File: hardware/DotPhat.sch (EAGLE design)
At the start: 46 parts, among them CN1 1X4-BIG, IC1 CAT24M010TS, J2 RASPBERRYPI-40-PIN-GPIO_PTH, J3 USB-MICROB, U1 ATMEGA328P-MU-QFN32, U2 TMP102, U3 ATSHA204-TSU, U4 W25Q32FV, X2 MC-RTC-RV-4162-C7-I2C, X3 S4B-ZR

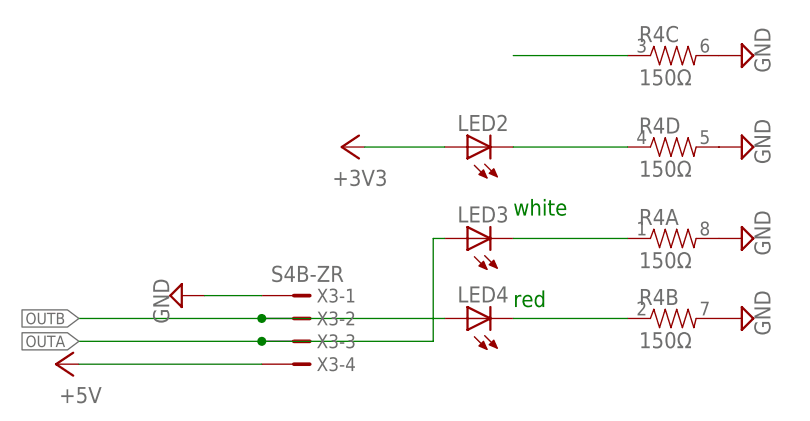
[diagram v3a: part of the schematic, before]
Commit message: Add jumper for power led
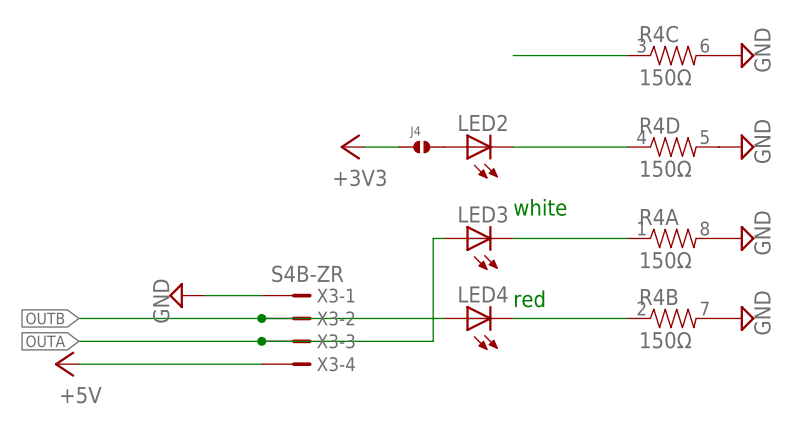
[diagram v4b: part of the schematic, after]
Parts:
- added J4: (no value), solderjumper:SOLDERJUMPER.2.MED
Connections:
- new net N$12: J4.2, LED2.A
- net +3V3: now also J4.1; no longer LED2.A
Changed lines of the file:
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@@
 <setting verticaltext="up"/>
 </settings>
-<grid distance="0.1" unitdist="inch" unit="inch" style="lines" multiple="1" display="no" altdistance="0.01" altunitdist="inch" altunit="inch"/>
+<grid distance="0.05" unitdist="inch" unit="inch" style="lines" multiple="1" display="no" altdistance="0.01" altunitdist="inch" altunit="inch"/>
 <layers>
 <layer number="1" name="Top" color="4" fill="1" visible="no" active="no"/>
@@
 <part name="IC2" library="MCP1700" deviceset="MCP1700" device="TT"/>
 <part name="C9" library="rcl" deviceset="C-EU" device="C0603" value="1uF"/>
+<part name="J4" library="solderjumper" deviceset="SOLDERJUMPER.2" device=".MED"/>
 </parts>
 <sheets>
@@
 <instance part="IC2" gate="G$1" x="144.78" y="-35.56"/>
 <instance part="C9" gate="G$1" x="134.62" y="-38.1"/>
+<instance part="J4" gate="G$1" x="124.46" y="142.24"/>
 </instances>
 <busses>
@@
 </segment>
 <segment>
-<pinref part="+3V1" gate="G$1" pin="+3V3"/>
-<wire x1="127" y1="142.24" x2="118.11" y2="142.24" width="0.1524" layer="91"/>
-<pinref part="LED2" gate="G$1" pin="A"/>
-</segment>
-<segment>
 <pinref part="CN1" gate="G$1" pin="3"/>
 <wire x1="76.2" y1="-77.47" x2="68.58" y2="-77.47" width="0.1524" layer="91"/>
@@
 <wire x1="53.34" y1="-119.38" x2="73.66" y2="-119.38" width="0.1524" layer="91"/>
 <wire x1="73.66" y1="-119.38" x2="73.66" y2="-116.84" width="0.1524" layer="91"/>
+</segment>
+<segment>
+<pinref part="J4" gate="G$1" pin="1"/>
+<pinref part="+3V1" gate="G$1" pin="+3V3"/>
+<wire x1="121.92" y1="142.24" x2="118.11" y2="142.24" width="0.1524" layer="91"/>
 </segment>
 </net>
@@
 </segment>
 </net>
+<net name="N$12" class="0">
+<segment>
+<pinref part="LED2" gate="G$1" pin="A"/>
+<pinref part="J4" gate="G$1" pin="2"/>
+</segment>
+</net>

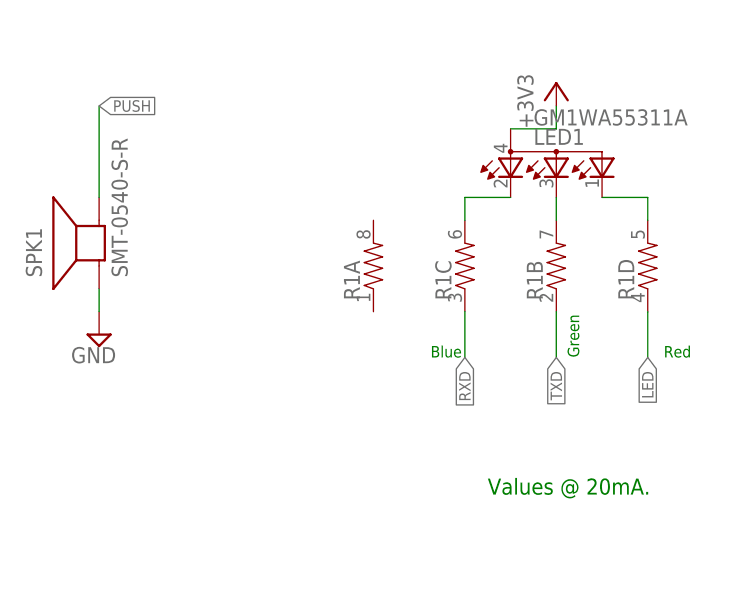
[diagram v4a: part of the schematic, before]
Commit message: Add radio activity led
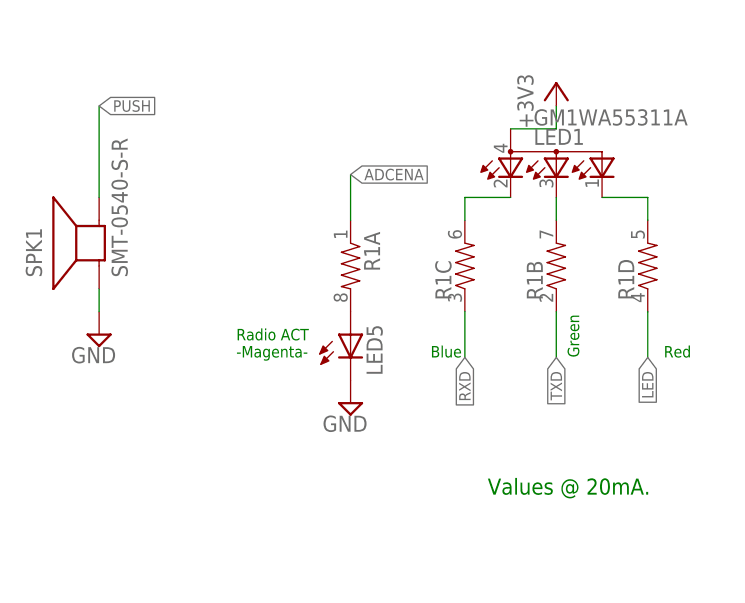
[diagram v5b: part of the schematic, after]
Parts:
- added LED5: (no value), SparkFun:LED0603
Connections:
- new net N$13: LED5.A, R1A.2
- net ADCENA: now also R1A.1
- net GND: now also LED5.C
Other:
- note added: "Radio ACT -Magenta-"
- moved on the sheet: R1A
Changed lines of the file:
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@@
 <setting verticaltext="up"/>
 </settings>
-<grid distance="0.05" unitdist="inch" unit="inch" style="lines" multiple="1" display="no" altdistance="0.01" altunitdist="inch" altunit="inch"/>
+<grid distance="0.1" unitdist="inch" unit="inch" style="lines" multiple="1" display="no" altdistance="0.01" altunitdist="inch" altunit="inch"/>
 <layers>
 <layer number="1" name="Top" color="4" fill="1" visible="no" active="no"/>
@@
 <part name="C9" library="rcl" deviceset="C-EU" device="C0603" value="1uF"/>
 <part name="J4" library="solderjumper" deviceset="SOLDERJUMPER.2" device=".MED"/>
+<part name="LED5" library="SparkFun" deviceset="LED" device="0603"/>
+<part name="SUPPLY28" library="supply2" deviceset="GND" device=""/>
 </parts>
 <sheets>
@@
 <text x="254" y="7.62" size="1.27" layer="91" rot="R90">needs Pullup for INT pin</text>
 <text x="66.04" y="-114.3" size="1.27" layer="91" rot="R90">needs Pullup for INT pin</text>
+<text x="-58.42" y="50.8" size="1.27" layer="91">Radio ACT
+-Magenta-</text>
 </plain>
 <instances>
@@
 <instance part="P+4" gate="1" x="134.62" y="-27.94"/>
 <instance part="C1" gate="G$1" x="154.94" y="-38.1"/>
-<instance part="R1" gate="A" x="-43.18" y="60.96" rot="R90"/>
+<instance part="R1" gate="A" x="-45.72" y="60.96" rot="R270"/>
 <instance part="R1" gate="B" x="-22.86" y="60.96" rot="R90"/>
 <instance part="R1" gate="C" x="-33.02" y="60.96" rot="R90"/>
@@
 <instance part="C9" gate="G$1" x="134.62" y="-38.1"/>
 <instance part="J4" gate="G$1" x="124.46" y="142.24"/>
+<instance part="LED5" gate="G$1" x="-45.72" y="53.34"/>
+<instance part="SUPPLY28" gate="GND" x="-45.72" y="45.72" rot="MR0"/>
 </instances>
 <busses>
@@
 <pinref part="SUPPLY27" gate="GND" pin="GND"/>
 </segment>
+<segment>
+<pinref part="LED5" gate="G$1" pin="C"/>
+<pinref part="SUPPLY28" gate="GND" pin="GND"/>
+</segment>
 </net>
 <net name="SDA" class="0">
@@
 <junction x="132.08" y="-160.02"/>
 </segment>
+<segment>
+<pinref part="R1" gate="A" pin="1"/>
+<wire x1="-45.72" y1="66.04" x2="-45.72" y2="71.12" width="0.1524" layer="91"/>
+<label x="-45.72" y="71.12" size="1.27" layer="95" xref="yes"/>
+</segment>
 </net>
 <net name="MOSI" class="0">
@@
 </segment>
 </net>
+<net name="N$13" class="0">
+<segment>
+<pinref part="R1" gate="A" pin="2"/>
+<pinref part="LED5" gate="G$1" pin="A"/>
+</segment>
+</net>

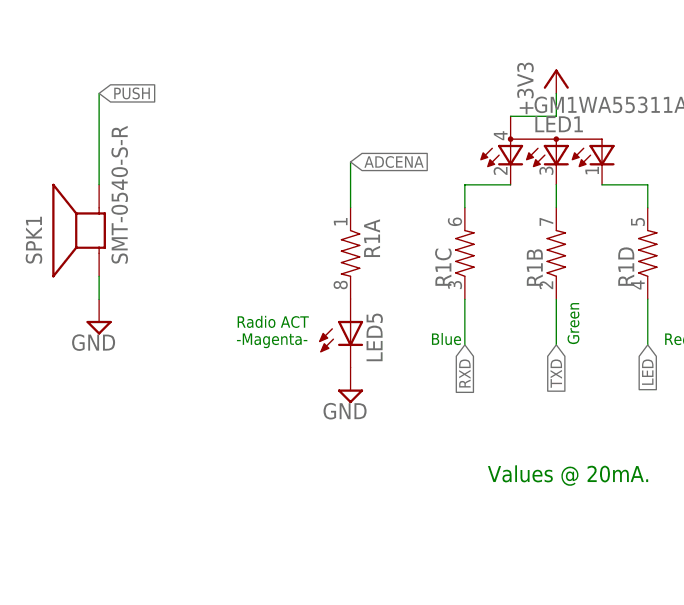
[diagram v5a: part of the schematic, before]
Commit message: Add TRx leds for radio communication, improve GND
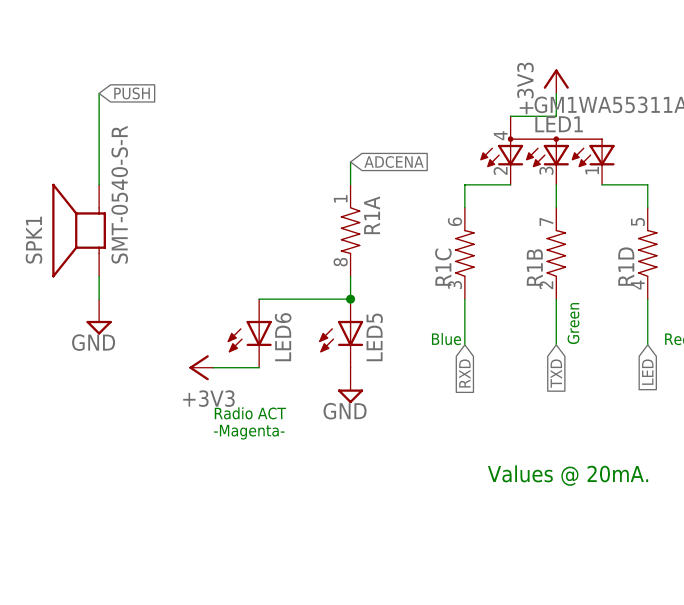
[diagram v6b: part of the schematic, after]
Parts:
- added LED6: (no value), SparkFun:LED0603
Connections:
- net +3V3: now also LED6.C
- net N$13: now also LED6.A
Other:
- moved on the sheet: R1A
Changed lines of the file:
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@@
 <part name="LED5" library="SparkFun" deviceset="LED" device="0603"/>
 <part name="SUPPLY28" library="supply2" deviceset="GND" device=""/>
+<part name="LED6" library="SparkFun" deviceset="LED" device="0603"/>
+<part name="+3V21" library="supply1" deviceset="+3V3" device=""/>
 </parts>
 <sheets>
@@
 <text x="254" y="7.62" size="1.27" layer="91" rot="R90">needs Pullup for INT pin</text>
 <text x="66.04" y="-114.3" size="1.27" layer="91" rot="R90">needs Pullup for INT pin</text>
-<text x="-58.42" y="50.8" size="1.27" layer="91">Radio ACT
+<text x="-60.96" y="40.64" size="1.27" layer="91">Radio ACT
 -Magenta-</text>
 </plain>
@@
 <instance part="P+4" gate="1" x="134.62" y="-27.94"/>
 <instance part="C1" gate="G$1" x="154.94" y="-38.1"/>
-<instance part="R1" gate="A" x="-45.72" y="60.96" rot="R270"/>
+<instance part="R1" gate="A" x="-45.72" y="63.5" rot="R270"/>
 <instance part="R1" gate="B" x="-22.86" y="60.96" rot="R90"/>
 <instance part="R1" gate="C" x="-33.02" y="60.96" rot="R90"/>
@@
 <instance part="LED5" gate="G$1" x="-45.72" y="53.34"/>
 <instance part="SUPPLY28" gate="GND" x="-45.72" y="45.72" rot="MR0"/>
+<instance part="LED6" gate="G$1" x="-55.88" y="53.34"/>
+<instance part="+3V21" gate="G$1" x="-63.5" y="48.26" rot="R90"/>
 </instances>
 <busses>
@@
 <wire x1="121.92" y1="142.24" x2="118.11" y2="142.24" width="0.1524" layer="91"/>
 </segment>
+<segment>
+<pinref part="LED6" gate="G$1" pin="C"/>
+<pinref part="+3V21" gate="G$1" pin="+3V3"/>
+<wire x1="-55.88" y1="48.26" x2="-60.96" y2="48.26" width="0.1524" layer="91"/>
+</segment>
 </net>
 <net name="ADCENA" class="0">
@@
 <segment>
 <pinref part="R1" gate="A" pin="1"/>
-<wire x1="-45.72" y1="66.04" x2="-45.72" y2="71.12" width="0.1524" layer="91"/>
+<wire x1="-45.72" y1="68.58" x2="-45.72" y2="71.12" width="0.1524" layer="91"/>
 <label x="-45.72" y="71.12" size="1.27" layer="95" xref="yes"/>
 </segment>
@@
 <pinref part="R1" gate="A" pin="2"/>
 <pinref part="LED5" gate="G$1" pin="A"/>
-</segment>
-</net>
+<wire x1="-45.72" y1="58.42" x2="-45.72" y2="55.88" width="0.1524" layer="91"/>
+<pinref part="LED6" gate="G$1" pin="A"/>
+<wire x1="-55.88" y1="55.88" x2="-45.72" y2="55.88" width="0.1524" layer="91"/>
+<junction x="-45.72" y="55.88"/>
+</segment>
+</net>

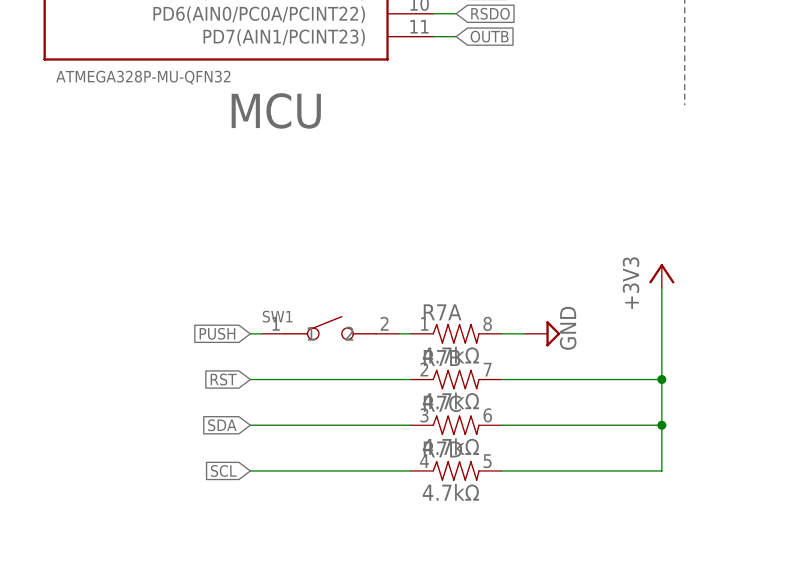
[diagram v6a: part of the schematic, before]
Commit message: Add push reset and action
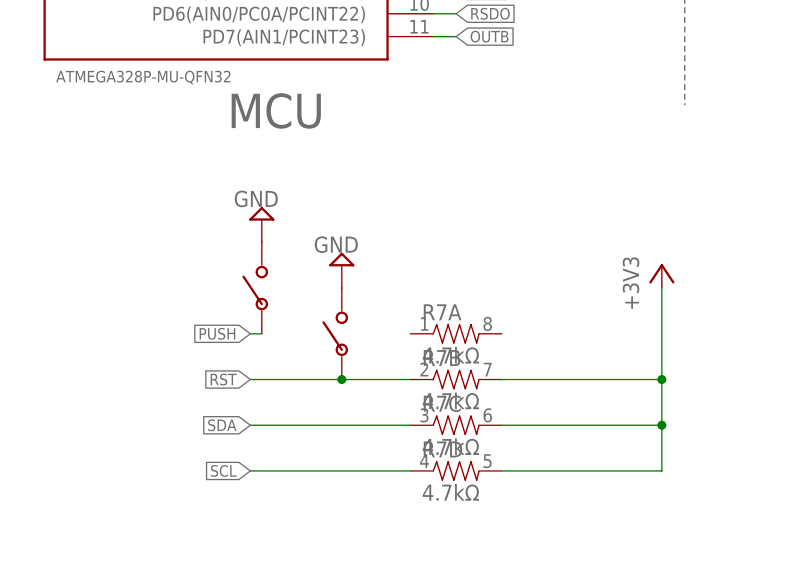
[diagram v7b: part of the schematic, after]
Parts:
- removed SW1: (no value), Seeed-OPL-Switch:SMD-BUTTON(2P-6.0X3.0X2.5MM)-DHT-1163S
- added U$2, U$3: PUSHBUTTON_4X2.5, pusbbutton_4x2_5:PUSHBUTTON_4X2.5
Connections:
- removed net N$5: R7A.1, SW1.2
- net GND: now also U$2.P$2, U$3.P$2; no longer R7A.2
- net PUSH: now also U$3.P$1; no longer SW1.1
- net RST: now also U$2.P$1
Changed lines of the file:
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@@
 <setting verticaltext="up"/>
 </settings>
-<grid distance="0.1" unitdist="inch" unit="inch" style="lines" multiple="1" display="no" altdistance="0.01" altunitdist="inch" altunit="inch"/>
+<grid distance="0.05" unitdist="inch" unit="inch" style="lines" multiple="1" display="no" altdistance="0.01" altunitdist="inch" altunit="inch"/>
 <layers>
 <layer number="1" name="Top" color="4" fill="1" visible="no" active="no"/>
@@
 <part name="R7" library="SparkFun" deviceset="RESISTOR-ARRAY" device="0603-ARV" value="4.7kΩ"/>
 <part name="+3V8" library="supply1" deviceset="+3V3" device=""/>
-<part name="SW1" library="Seeed-OPL-Switch" deviceset="SMD-BUTTON(2P-6.0X3.0X2.5MM)" device="-DHT-1163S"/>
-<part name="SUPPLY19" library="supply2" deviceset="GND" device=""/>
 <part name="+3V3" library="supply1" deviceset="+3V3" device=""/>
 <part name="SUPPLY1" library="supply2" deviceset="GND" device=""/>
@@
 <part name="LED6" library="SparkFun" deviceset="LED" device="0603"/>
 <part name="+3V21" library="supply1" deviceset="+3V3" device=""/>
+<part name="SUPPLY31" library="supply2" deviceset="GND" device=""/>
+<part name="U$2" library="pusbbutton_4x2_5" deviceset="PUSHBUTTON_4X2.5" device=""/>
+<part name="SUPPLY32" library="supply2" deviceset="GND" device=""/>
+<part name="U$3" library="pusbbutton_4x2_5" deviceset="PUSHBUTTON_4X2.5" device=""/>
 </parts>
 <sheets>
@@
 <instance part="R7" gate="D" x="78.74" y="-25.4"/>
 <instance part="+3V8" gate="G$1" x="101.6" y="-2.54"/>
-<instance part="SW1" gate="G$1" x="64.77" y="-10.16"/>
-<instance part="SUPPLY19" gate="GND" x="88.9" y="-10.16" rot="R90"/>
 <instance part="+3V3" gate="G$1" x="-16.51" y="-10.16"/>
 <instance part="SUPPLY1" gate="GND" x="-12.7" y="-63.5"/>
@@
 <instance part="LED6" gate="G$1" x="-55.88" y="53.34"/>
 <instance part="+3V21" gate="G$1" x="-63.5" y="48.26" rot="R90"/>
+<instance part="SUPPLY31" gate="GND" x="66.04" y="-2.54" rot="R180"/>
+<instance part="U$2" gate="G$1" x="66.04" y="-10.16" rot="R90"/>
+<instance part="SUPPLY32" gate="GND" x="57.15" y="2.54" rot="R180"/>
+<instance part="U$3" gate="G$1" x="57.15" y="-5.08" rot="R90"/>
 </instances>
 <busses>
@@
 <pinref part="Y1" gate="G$1" pin="2"/>
 <pinref part="SUPPLY30" gate="GND" pin="GND"/>
-</segment>
-<segment>
-<pinref part="R7" gate="A" pin="2"/>
-<pinref part="SUPPLY19" gate="GND" pin="GND"/>
-<wire x1="83.82" y1="-10.16" x2="86.36" y2="-10.16" width="0.1524" layer="91"/>
 </segment>
 <segment>
@@
 <pinref part="SUPPLY28" gate="GND" pin="GND"/>
 </segment>
+<segment>
+<pinref part="U$2" gate="G$1" pin="P$2"/>
+<pinref part="SUPPLY31" gate="GND" pin="GND"/>
+</segment>
+<segment>
+<pinref part="U$3" gate="G$1" pin="P$2"/>
+<pinref part="SUPPLY32" gate="GND" pin="GND"/>
+</segment>
 </net>
 <net name="SDA" class="0">
@@
 <segment>
 <pinref part="R7" gate="B" pin="1"/>
-<wire x1="73.66" y1="-15.24" x2="55.88" y2="-15.24" width="0.1524" layer="91"/>
 <label x="55.88" y="-15.24" size="1.27" layer="95" rot="R180" xref="yes"/>
+<pinref part="U$2" gate="G$1" pin="P$1"/>
+<wire x1="73.66" y1="-15.24" x2="66.04" y2="-15.24" width="0.1524" layer="91"/>
+<wire x1="66.04" y1="-15.24" x2="55.88" y2="-15.24" width="0.1524" layer="91"/>
+<junction x="66.04" y="-15.24"/>
 </segment>
 <segment>
@@
 </segment>
 <segment>
-<pinref part="SW1" gate="G$1" pin="1"/>
 <wire x1="57.15" y1="-10.16" x2="55.88" y2="-10.16" width="0.1524" layer="91"/>
 <label x="55.88" y="-10.16" size="1.27" layer="95" rot="R180" xref="yes"/>
+<pinref part="U$3" gate="G$1" pin="P$1"/>
 </segment>
 <segment>
@@
 </segment>
 </net>
-<net name="N$5" class="0">
-<segment>
-<pinref part="R7" gate="A" pin="1"/>
-<pinref part="SW1" gate="G$1" pin="2"/>
-<wire x1="72.39" y1="-10.16" x2="73.66" y2="-10.16" width="0.1524" layer="91"/>
-</segment>
-</net>

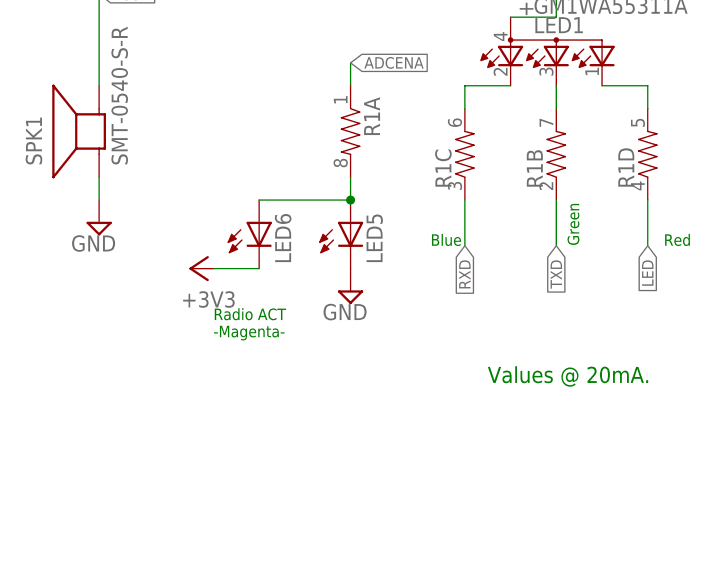
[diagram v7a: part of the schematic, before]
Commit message: Correct Rx led polarity
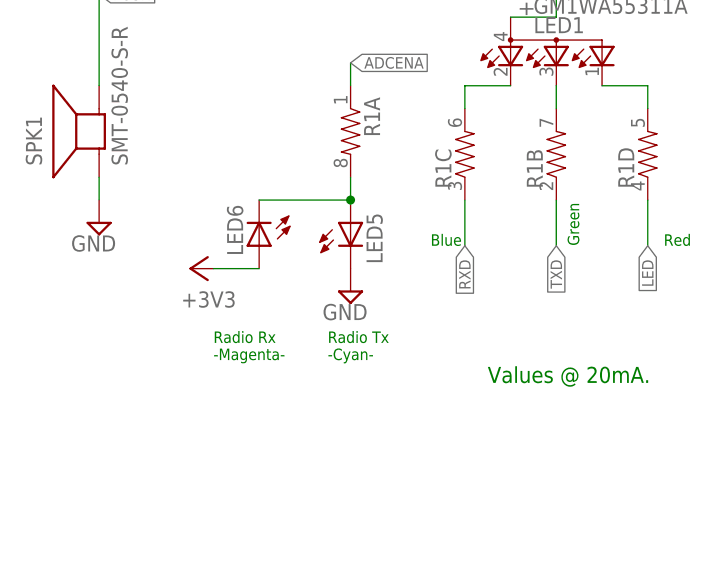
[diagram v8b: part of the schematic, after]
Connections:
- net +3V3: now also LED6.A; no longer LED6.C
- net N$13: now also LED6.C; no longer LED6.A
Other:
- note added: "Radio Rx -Magenta-"
- note added: "Radio Tx -Cyan-"
- note removed: "Radio ACT -Magenta-"
- moved on the sheet: LED6
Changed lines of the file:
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@@
 <setting verticaltext="up"/>
 </settings>
-<grid distance="0.05" unitdist="inch" unit="inch" style="lines" multiple="1" display="no" altdistance="0.01" altunitdist="inch" altunit="inch"/>
+<grid distance="0.1" unitdist="inch" unit="inch" style="lines" multiple="1" display="no" altdistance="0.01" altunitdist="inch" altunit="inch"/>
 <layers>
 <layer number="1" name="Top" color="4" fill="1" visible="no" active="no"/>
@@
 <text x="254" y="7.62" size="1.27" layer="91" rot="R90">needs Pullup for INT pin</text>
 <text x="66.04" y="-114.3" size="1.27" layer="91" rot="R90">needs Pullup for INT pin</text>
-<text x="-60.96" y="40.64" size="1.27" layer="91">Radio ACT
+<text x="-60.96" y="38.1" size="1.27" layer="91">Radio Rx
 -Magenta-</text>
+<text x="-48.26" y="38.1" size="1.27" layer="91">Radio Tx
+-Cyan-</text>
 </plain>
 <instances>
@@
 <instance part="LED5" gate="G$1" x="-45.72" y="53.34"/>
 <instance part="SUPPLY28" gate="GND" x="-45.72" y="45.72" rot="MR0"/>
-<instance part="LED6" gate="G$1" x="-55.88" y="53.34"/>
+<instance part="LED6" gate="G$1" x="-55.88" y="50.8" rot="R180"/>
 <instance part="+3V21" gate="G$1" x="-63.5" y="48.26" rot="R90"/>
 <instance part="SUPPLY31" gate="GND" x="66.04" y="-2.54" rot="R180"/>
@@
 </segment>
 <segment>
-<pinref part="LED6" gate="G$1" pin="C"/>
 <pinref part="+3V21" gate="G$1" pin="+3V3"/>
-<wire x1="-55.88" y1="48.26" x2="-60.96" y2="48.26" width="0.1524" layer="91"/>
+<pinref part="LED6" gate="G$1" pin="A"/>
+<wire x1="-60.96" y1="48.26" x2="-55.88" y2="48.26" width="0.1524" layer="91"/>
 </segment>
 </net>
@@
 <pinref part="LED5" gate="G$1" pin="A"/>
 <wire x1="-45.72" y1="58.42" x2="-45.72" y2="55.88" width="0.1524" layer="91"/>
-<pinref part="LED6" gate="G$1" pin="A"/>
+<pinref part="LED6" gate="G$1" pin="C"/>
 <wire x1="-55.88" y1="55.88" x2="-45.72" y2="55.88" width="0.1524" layer="91"/>
 <junction x="-45.72" y="55.88"/>
